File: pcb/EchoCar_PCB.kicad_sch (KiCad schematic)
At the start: 20 parts, among them J1 SW, J2 Display_Con, SW1 SW_SPDT, U1 STM32F103C8T6, U2 AMS1117-3.3, Y1 16MHz

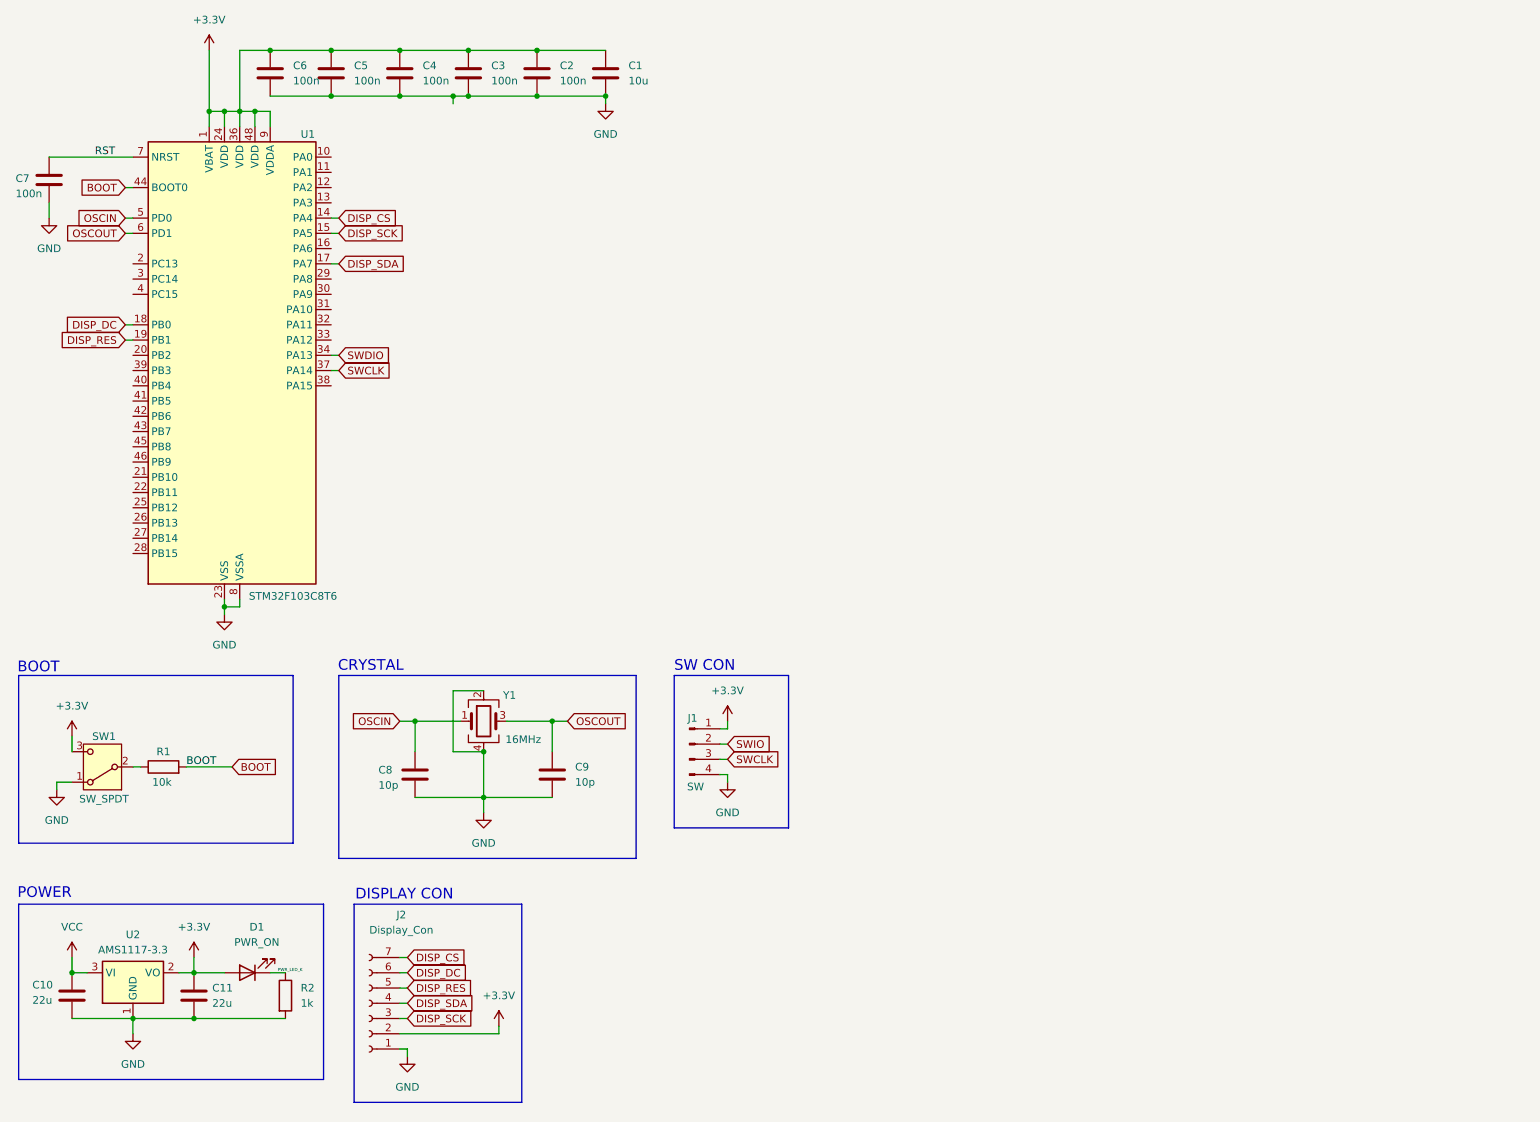
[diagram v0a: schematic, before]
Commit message: feat: Add the motor driver.
Add the motor driver to the schematic.

Signed-off-by: Victor Lima <vhsl@ic.ufal.br>
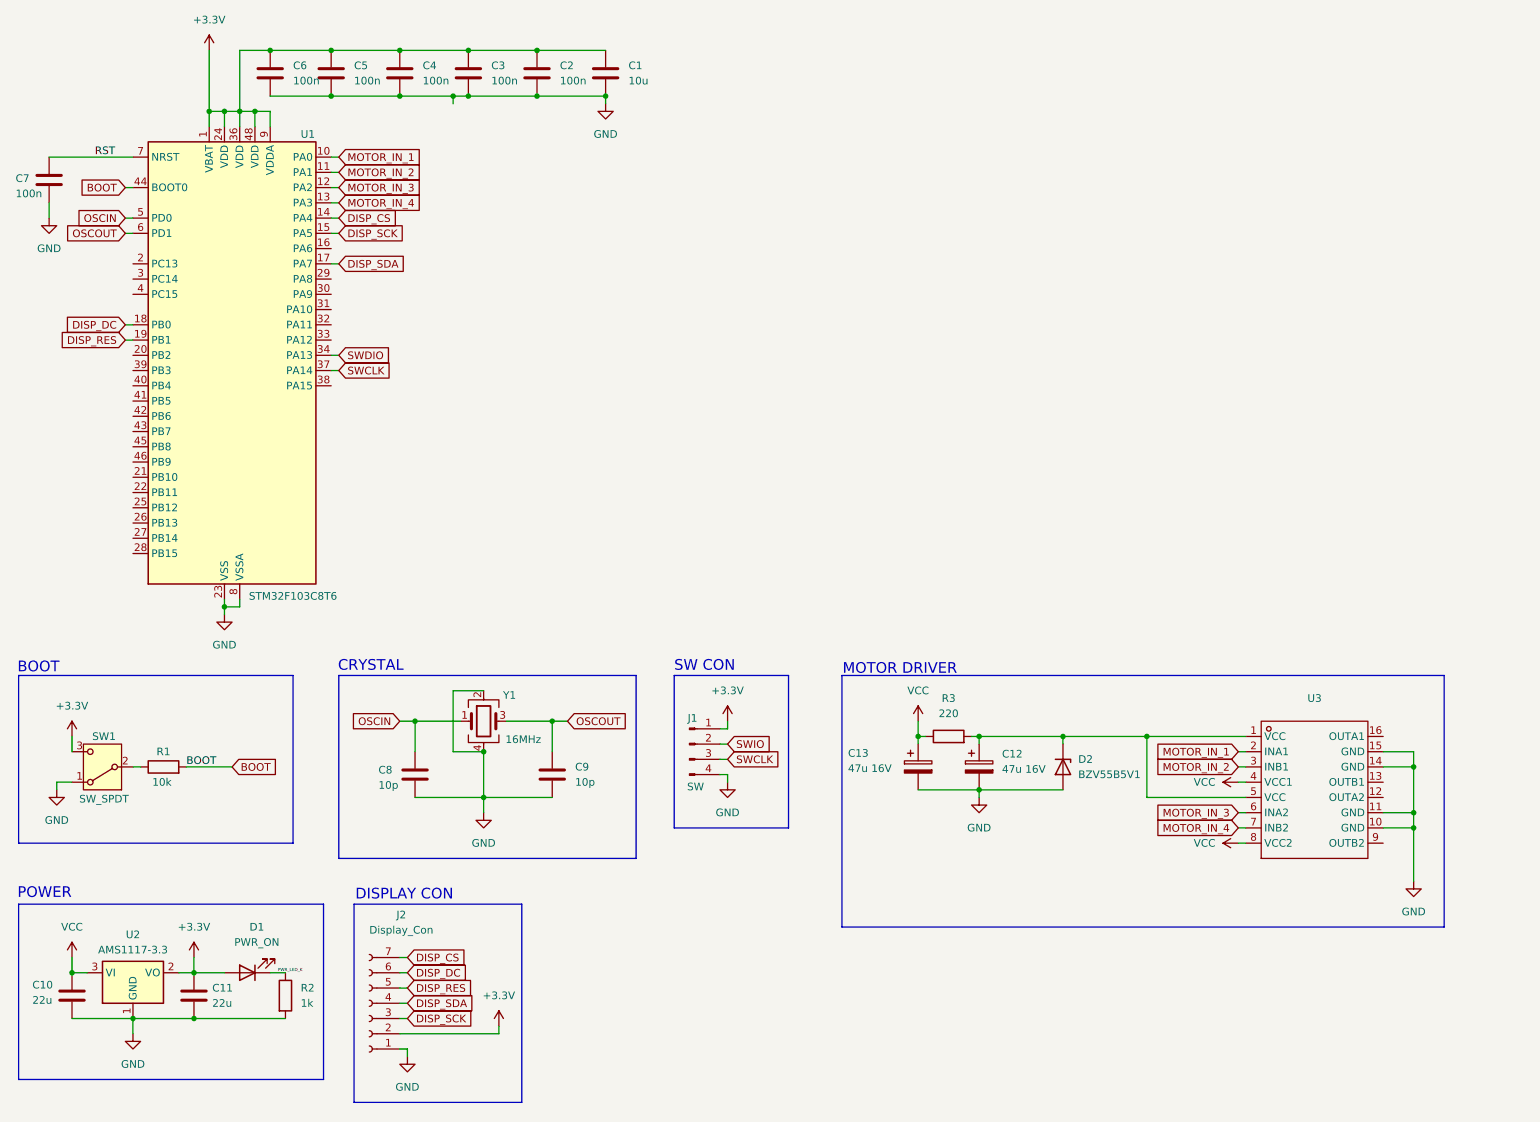
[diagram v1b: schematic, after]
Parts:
- added C12, C13: 47u 16V, symbol Device:C_Polarized
- added D2: BZV55B5V1, Diode_SMD:D_MiniMELF, symbol Diode:BZV55B5V1
- added R3: 220, symbol Device:R
- added U3: ~, MX1616H_SMD:MX1616H, symbol MX1616H_symbol:MX1616H
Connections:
- net GND: now also C12.2, C13.2, D2.2 (A), U3.10 (GND), U3.11 (GND), U3.14 (GND), U3.15 (GND)
- net VCC: now also C13.1, R3.1, U3.4 (VCC1), U3.8 (VCC2)
- net MOTOR_IN_1: now reaches U1.10 (PA0)
- net MOTOR_IN_1: now also U3.2 (INA1)
- net MOTOR_IN_2: now reaches U1.11 (PA1)
- net MOTOR_IN_2: now also U3.3 (INB1)
- net MOTOR_IN_3: now reaches U1.12 (PA2)
- net MOTOR_IN_3: now also U3.6 (INA2)
- net MOTOR_IN_4: now reaches U1.13 (PA3)
- net MOTOR_IN_4: now also U3.7 (INB2)
- new net: C12.1, D2.1 (K), R3.2, U3.1 (VCC), U3.5 (VCC)
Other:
- note added: "MOTOR DRIVER"

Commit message: feat: Conclude the schematic.
Conclude the pcb schematic and add the BOM.

Signed-off-by: Victor Lima <vhsl@ic.ufal.br>
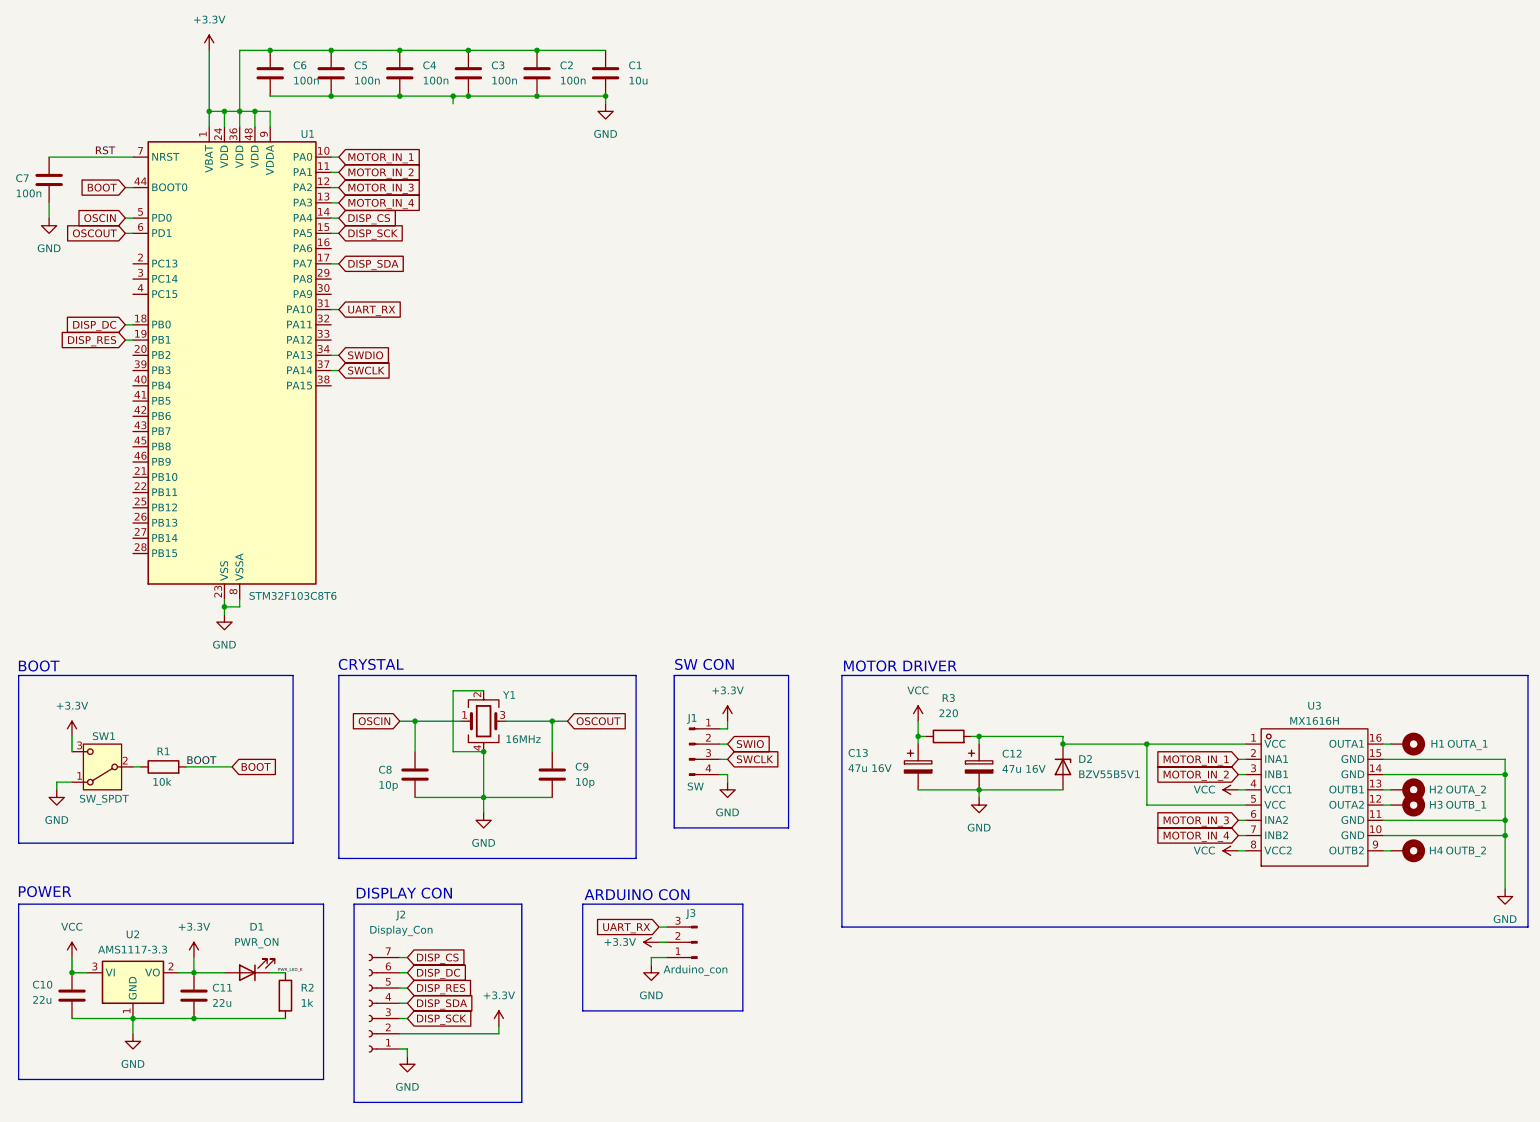
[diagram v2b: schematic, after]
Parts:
- added H1: OUTA_1, Connector_PinHeader_2.54mm:PinHeader_1x01_P2.54mm_Vertical, symbol Mechanical:MountingHole_Pad
- added H2: OUTA_2, Connector_PinHeader_2.54mm:PinHeader_1x01_P2.54mm_Vertical, symbol Mechanical:MountingHole_Pad
- added H3: OUTB_1, Connector_PinHeader_2.54mm:PinHeader_1x01_P2.54mm_Vertical, symbol Mechanical:MountingHole_Pad
- added H4: OUTB_2, Connector_PinHeader_2.54mm:PinHeader_1x01_P2.54mm_Vertical, symbol Mechanical:MountingHole_Pad
- added J3: Arduino_con, Connector_PinHeader_2.54mm:PinHeader_1x03_P2.54mm_Vertical, symbol Connector:Conn_01x03_Pin
- C1, C10, C11: footprint (none) -> Capacitor_SMD:C_0805_2012Metric
- C12, C13: footprint (none) -> Capacitor_SMD:CP_Elec_5x5.3
- C2, C3, C4, C5, C6, C7, C8, C9: footprint (none) -> Capacitor_SMD:C_0402_1005Metric
- D1: footprint (none) -> LED_SMD:LED_0603_1608Metric
- J1: footprint (none) -> Connector_PinHeader_2.54mm:PinHeader_1x04_P2.54mm_Vertical
- J2: footprint (none) -> Connector_PinSocket_2.54mm:PinSocket_1x07_P2.54mm_Vertical
- R1, R2, R3: footprint (none) -> Resistor_SMD:R_0402_1005Metric
- SW1: footprint (none) -> Button_Switch_THT:SW_E-Switch_EG1224_SPDT_Angled
- U3: value ~ -> MX1616H
- Y1: footprint (none) -> Crystal:Crystal_SMD_3225-4Pin_3.2x2.5mm
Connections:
- net +3.3V: now also J3.2 (Pin_2)
- net GND: now also J3.1 (Pin_1)
- net UART_RX: now reaches U1.31 (PA10)
- net UART_RX: now also J3.3 (Pin_3)
- net at U3.12 (OUTA2): now also H3.1
- net at U3.13 (OUTB1): now also H2.1
- net at U3.16 (OUTA1): now also H1.1
- net at U3.9 (OUTB2): now also H4.1
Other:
- note added: "ARDUINO CON"
- moved on the sheet: U3

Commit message: feat: Finish the PCB.
Finish the project PCB.

Signed-off-by: Victor Lima <vhsl@ic.ufal.br>
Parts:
- added H5: VCC, Connector_PinHeader_2.54mm:PinHeader_1x01_P2.54mm_Vertical, symbol Mechanical:MountingHole_Pad
- added H6: GND, Connector_PinHeader_2.54mm:PinHeader_1x01_P2.54mm_Vertical, symbol Mechanical:MountingHole_Pad
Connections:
- net SWDIO is gone; now on net SWIO: U1.34 (PA13)
- net GND: now also H6.1
- net VCC: now also H5.1
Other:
- note added: "POWER HOLE"
- moved on the sheet: C5
